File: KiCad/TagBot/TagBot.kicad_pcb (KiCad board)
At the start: 4 copper layers, 54 x 57 mm, 81 parts, among them IC101 ADXL343BCCZ-RL, J1001 Conn_01x06, J1002 Conn_01x06, J101 Conn_ST_STDC14, J103 Conn_01x03, J105 Conn_01x02, J1101 Conn_01x04, J801 Conn_01x06, J901 Conn_01x08, SW701 SW_Push, SW702 SW_Push, U101 STM32G431CBUx, U201 ZXBM5210-SP, U301 ZXBM5210-SP, U401 MP1475S, U501 BU33SD5WG-TR, Y101 Crystal

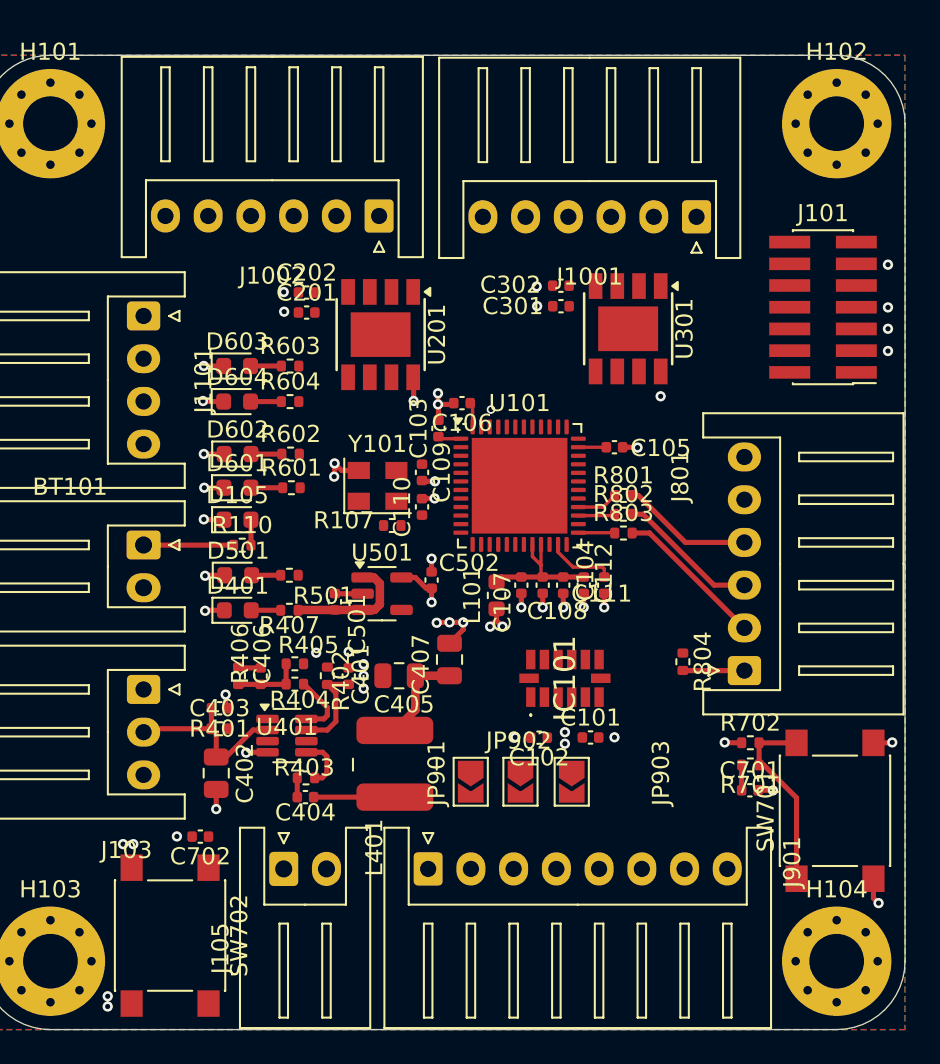
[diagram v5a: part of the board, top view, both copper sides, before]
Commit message: Routed data tracks
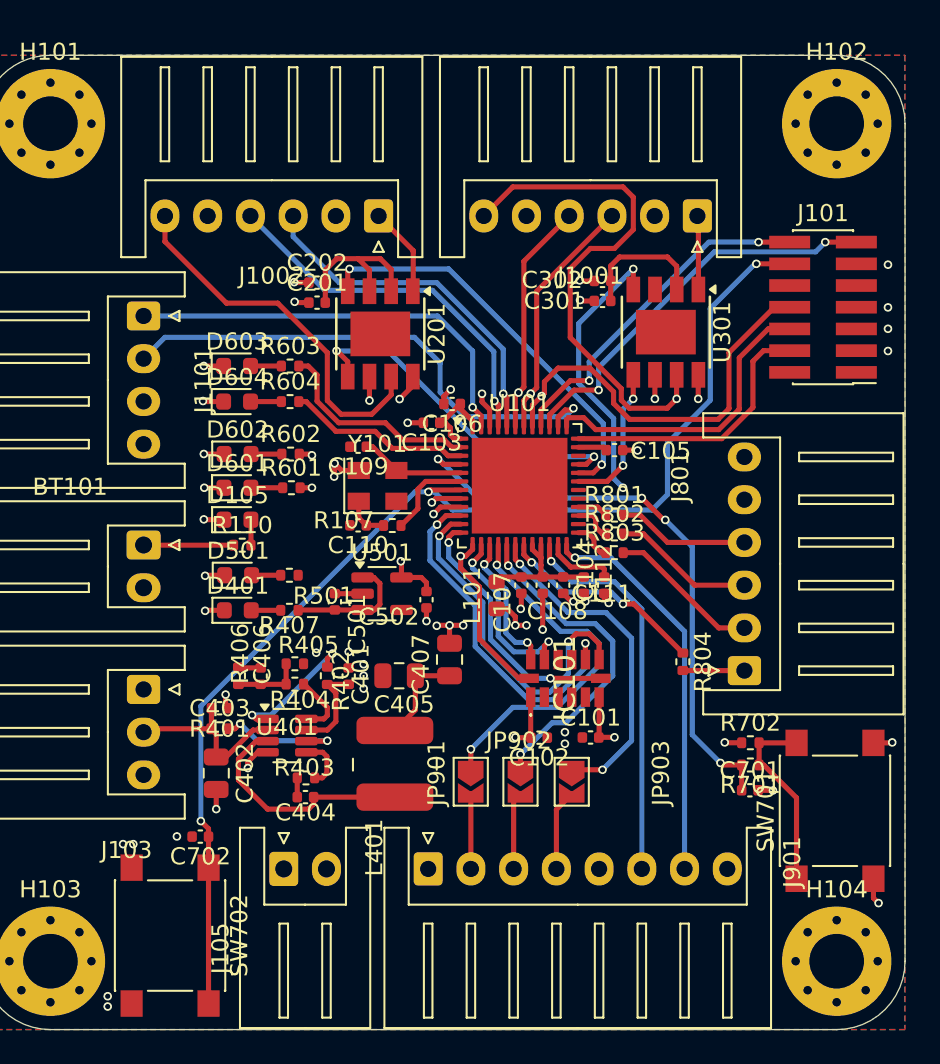
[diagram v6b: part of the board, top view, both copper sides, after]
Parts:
- moved C109 4.03 mm to (58.0, 58.9), turned to 180 degrees
- moved C110 3.89 mm to (58.0, 63.5), turned to 180 degrees
- moved C302 2.45 mm to (72.3, 49.2)
- moved C301 2.45 mm to (72.3, 50.4)
- moved U301 2.21 mm to (76.0, 52.2)
- moved R801 1.26 mm to (73.0, 62.9)
- moved R802 1.26 mm to (73.0, 64.0)
- moved R803 1.26 mm to (73.0, 65.1)
- moved C502 1.19 mm to (62.0, 67.8), turned to -90 degrees
- moved C202 0.84 mm to (55.6, 49.3)
- moved C201 0.84 mm to (55.6, 50.5)
- moved C106 0.58 mm to (63.5, 56.4)
- moved C103 0.52 mm to (62.3, 57.5), turned to 180 degrees
- moved C105 0.17 mm to (73.0, 59.1)
- moved J1001 0.07 mm to (77.8, 45.4)
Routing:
- net /NRST: track 0.00 -> 70.5 mm, vias 0 -> 3
- net /BTN_CAT_MOUSE: track 1.48 -> 34.5 mm, vias 0 -> 4
- net /OLED_SCL: track 0.00 -> 30.5 mm, vias 0 -> 1
- net /RIGHT_OUT2: track 0.00 -> 30.2 mm, vias 0 -> 1
- net /OLED_SDA: track 0.00 -> 24.7 mm, vias 0 -> 1
- net /LEFT_FWD: track 0.00 -> 23.9 mm, vias 0 -> 2
- net /SYS_JTDO-SWO: track 0.00 -> 23.9 mm, vias 0 -> 1
- net /STLINK_TX: track 0.00 -> 23.6 mm, vias 0 -> 2
- net /LIDAR_Output: track 0.00 -> 23.2 mm, vias 0 -> 1
- net /LIDAR_Input: track 0.00 -> 22.7 mm, vias 0 -> 1
- net /LEFT_OUT2: track 0.00 -> 22.1 mm
- net /Encoder_Left_B: track 0.00 -> 22.0 mm, vias 0 -> 1
- net /M_EN: track 0.00 -> 21.2 mm, vias 0 -> 2
- net /Interrupt1: track 0.00 -> 20.9 mm, vias 0 -> 2
- net /Encoder_Left_A: track 0.00 -> 20.9 mm, vias 0 -> 1
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
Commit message: update routage
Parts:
- moved L101 8.47 mm to (74.5, 68.8), turned to 180 degrees
- moved C108 8.12 mm to (74.7, 71.0)
- moved C111 7.02 mm to (75.8, 71.0)
- moved R804 3.00 mm to (74.2, 72.5), turned to 0 degrees
- moved C102 2.11 mm to (66.5, 75.5)
- moved C101 2.09 mm to (69.5, 75.5)
- moved IC101 2.01 mm to (68.1, 72.2)
- moved R801 0.61 mm to (72.9, 62.3)
- moved R802 0.61 mm to (72.9, 63.4)
- moved R803 0.61 mm to (72.9, 64.5)
- moved JP901 0.47 mm to (64.6, 79.0)
- moved JP902 0.47 mm to (67.5, 79.0)
- moved JP903 0.47 mm to (70.5, 79.0)
- moved C107 0.36 mm to (69.1, 66.8), turned to 180 degrees
- moved C112 0.34 mm to (70.9, 67.1), turned to -90 degrees
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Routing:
- net /USR_LED_1: track 2.56 -> 11.4 mm
- net /USR_LED_2: track 2.46 -> 10.2 mm
- net /Interrupt2: track 20.6 -> 13.1 mm
- net /Interrupt1: track 20.9 -> 14.1 mm
- net +3.3VA: track 8.16 -> 13.7 mm
- net Net-(J901-Pin_4): track 4.75 -> 0.00 mm
- net Net-(J901-Pin_3): track 4.54 -> 0.00 mm
- net Net-(J901-Pin_2): track 4.38 -> 0.00 mm
- net /Valim: track 30.9 -> 26.8 mm
- net Net-(J801-Pin_1): track 3.60 -> 0.00 mm
- net +3.3V: track 24.1 -> 27.6 mm, vias 7 -> 10
- net /SDO-MISO: track 10.9 -> 7.71 mm
- net /RIGHT_FWD: track 16.4 -> 19.1 mm
- net /LIDAR_Input: track 22.7 -> 25.3 mm, vias 1 -> 0
- net GND: track 39.4 -> 36.8 mm, vias 49 -> 59
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- added copper zone on In2.Cu, net +5V
- added copper zone on In2.Cu, net /Vbatterie

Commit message: update routage
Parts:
- moved D603 0.18 mm to (50.9, 54.0)
- moved R603 0.18 mm to (54.0, 54.0)
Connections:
- J1101 pad 3: +5V -> +3.3V
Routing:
- net +3.3V: track 27.6 -> 78.9 mm
- net GND: track 36.8 -> 63.9 mm, vias 59 -> 115
- net Net-(J103-Pin_3): track 0.00 -> 12.5 mm
- net /Valim: track 26.8 -> 38.0 mm, vias 2 -> 4
- net Net-(J801-Pin_1): track 0.00 -> 7.42 mm, vias 0 -> 2
- net /STLINK_RX: track 21.4 -> 27.4 mm
- net Net-(J901-Pin_4): track 0.00 -> 4.27 mm
- net Net-(J901-Pin_3): track 0.00 -> 4.07 mm
- net Net-(J901-Pin_2): track 0.00 -> 3.90 mm
- net +5V: track 15.2 -> 18.4 mm, vias 8 -> 7
- net /BTN_CAT_MOUSE: track 35.6 -> 38.6 mm
- net /RIGHT_OUT2: track 30.9 -> 32.6 mm
- net /SYS_JTDO-SWO: track 24.2 -> 23.2 mm
- net Net-(U401-EN/SYNC): track 7.56 -> 8.53 mm
- net /OLED_SCL: track 28.1 -> 27.2 mm
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- added copper zone on In2.Cu, net /Valim
- added copper zone on B.Cu, net /Vbatterie
